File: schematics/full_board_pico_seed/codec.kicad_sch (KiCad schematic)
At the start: 26 parts, among them J10 Conn_01x01_Female, J11 Conn_01x01_Female, U6 CS4270-CZZ, X1 SG-5032CAN

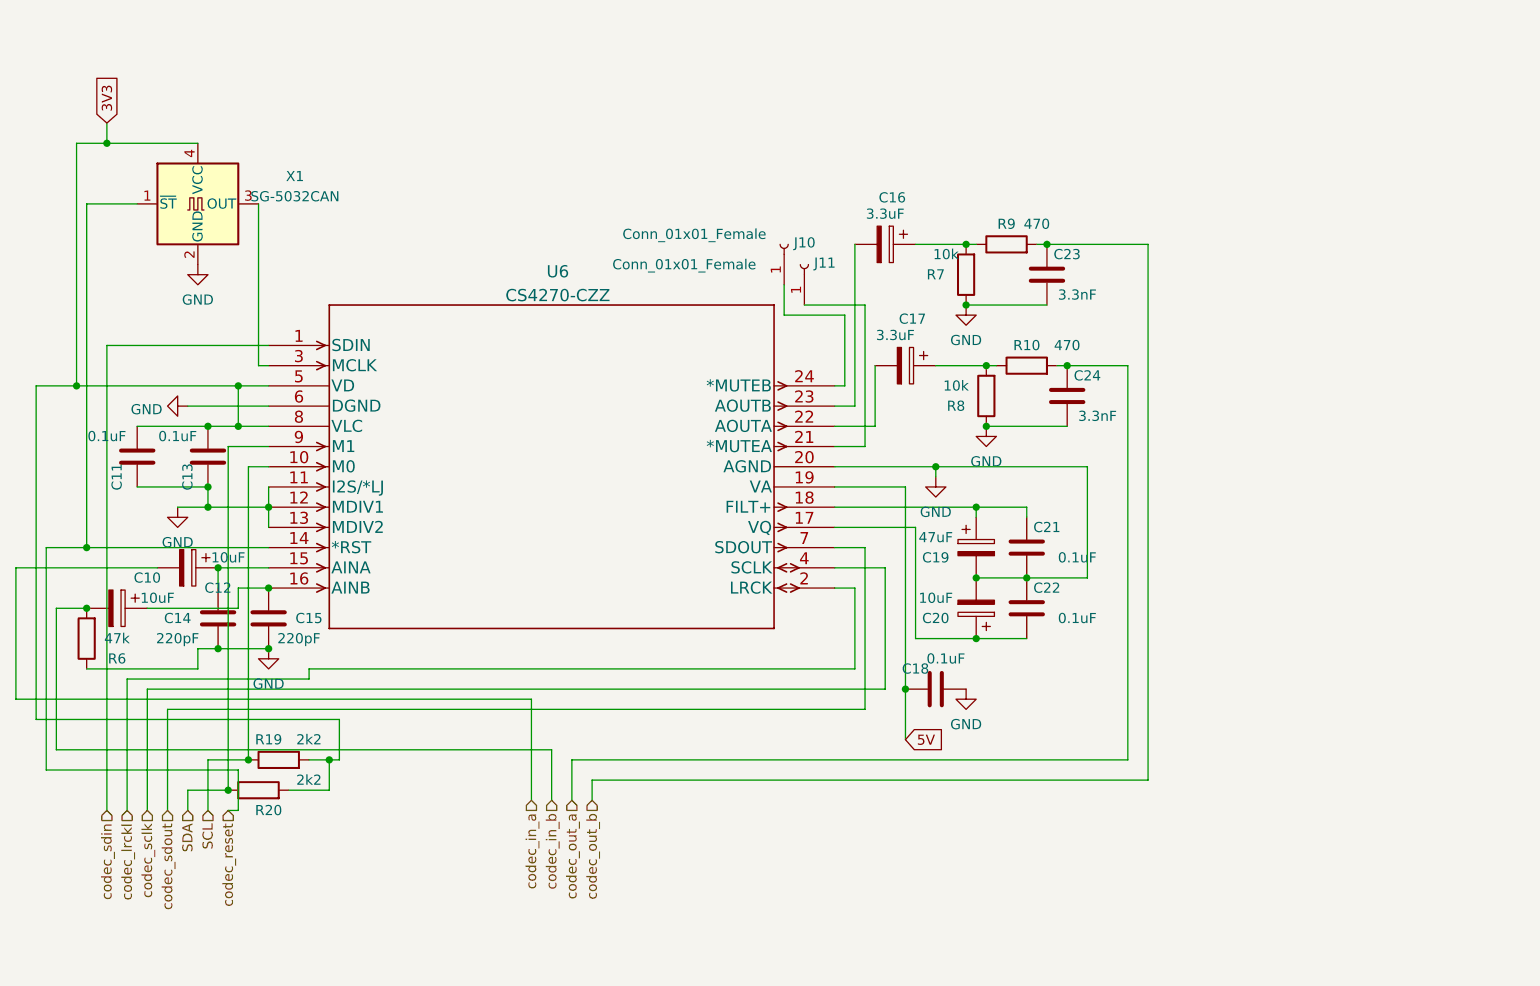
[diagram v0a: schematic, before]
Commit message: more work on full schematic: added test points
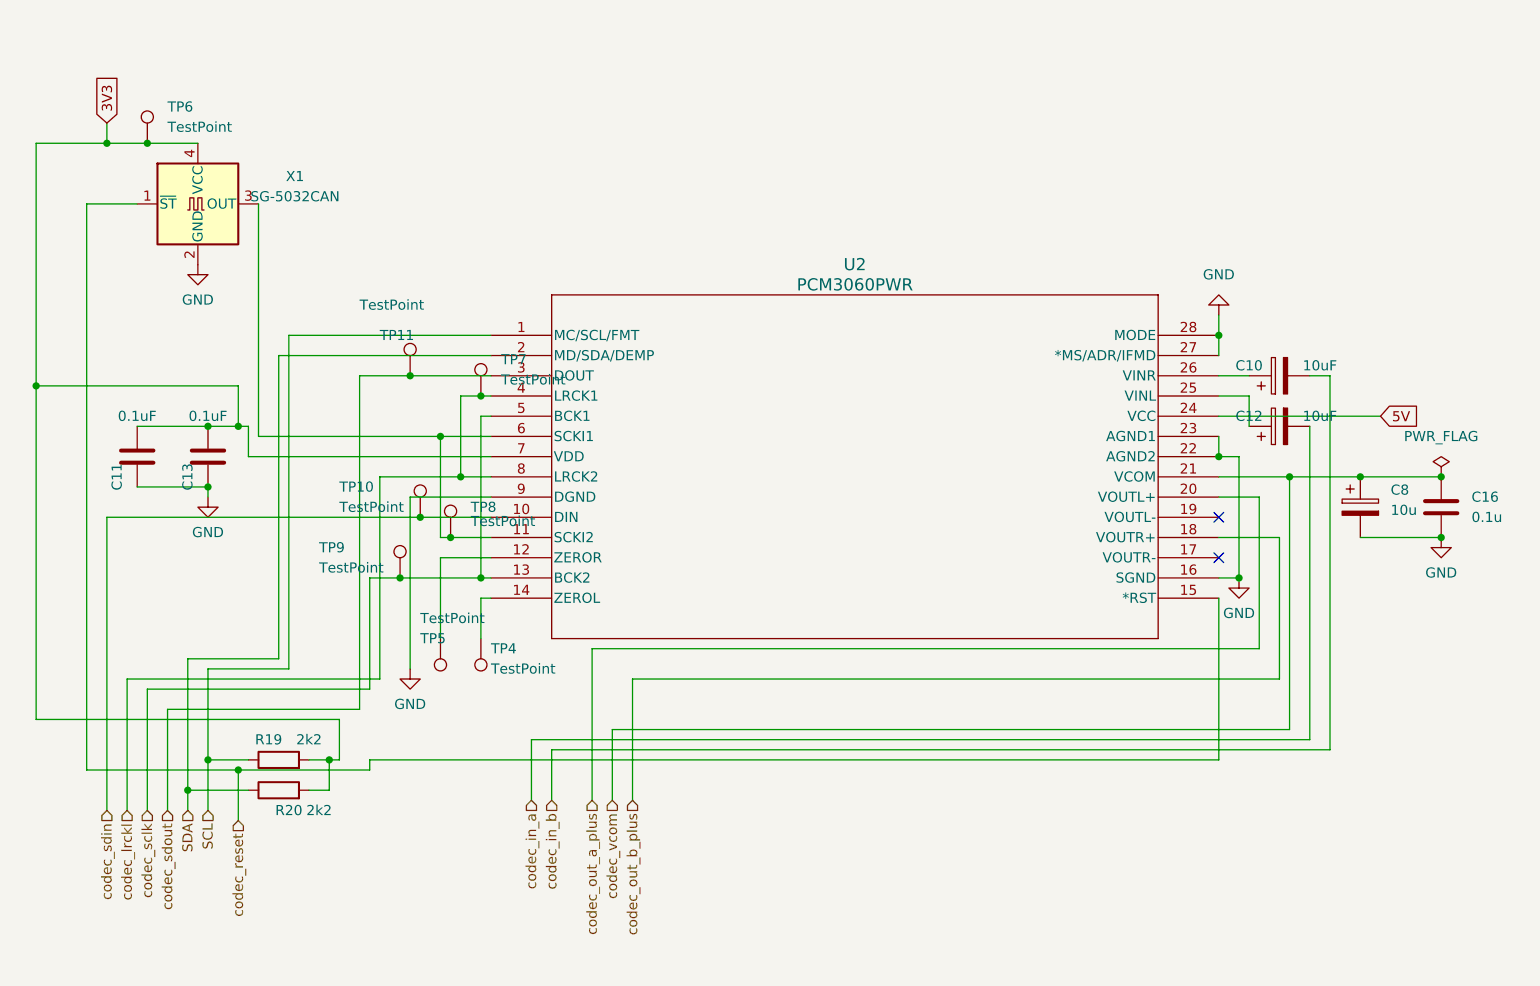
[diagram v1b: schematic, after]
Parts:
- removed C14, C15: 220pF, Capacitor_SMD:C_0603_1608Metric_Pad1.08x0.95mm_HandSolder, symbol Device:C
- removed C16, C17: 3.3uF, Capacitor_SMD:CP_Elec_4x4.5, symbol Device:C_Polarized
- removed C18, C21, C22: 0.1uF, Capacitor_SMD:C_1210_3225Metric_Pad1.33x2.70mm_HandSolder, symbol Device:C
- removed C19: 47uF, Capacitor_SMD:CP_Elec_5x5.4, symbol Device:C_Polarized
- removed C20: 10uF, Capacitor_SMD:CP_Elec_4x4.5, symbol Device:C_Polarized
- removed C23, C24: 3.3nF, Capacitor_SMD:C_0805_2012Metric_Pad1.18x1.45mm_HandSolder, symbol Device:C
- removed J10, J11: Conn_01x01_Female, Connector_Pin:Pin_D0.7mm_L6.5mm_W1.8mm_FlatFork, symbol Connector:Conn_01x01_Female
- removed R10, R9: 470, Resistor_SMD:R_0603_1608Metric_Pad0.98x0.95mm_HandSolder, symbol Device:R
- removed R6: 47k, Resistor_SMD:R_0603_1608Metric_Pad0.98x0.95mm_HandSolder, symbol Device:R
- removed R7, R8: 10k, Resistor_SMD:R_0603_1608Metric_Pad0.98x0.95mm_HandSolder, symbol Device:R
- removed U6: CS4270-CZZ, Package_SO:TSSOP-24_4.4x7.8mm_P0.65mm, symbol 2022-10-31_07-27-24:CS4270-CZZ
- added C16: 0.1u, Capacitor_SMD:C_0805_2012Metric_Pad1.18x1.45mm_HandSolder, symbol Device:C
- added C8: 10u, Capacitor_SMD:CP_Elec_4x4.5, symbol Device:C_Polarized
- added TP10, TP11, TP4, TP5, TP6, TP7, TP8, TP9: TestPoint, TestPoint:TestPoint_Pad_D1.5mm, symbol Connector:TestPoint
- added U2: PCM3060PWR, Package_SO:TSSOP-28_4.4x9.7mm_P0.65mm, symbol pcm3060:PCM3060PWR
- C11, C13: footprint Capacitor_SMD:C_1210_3225Metric_Pad1.33x2.70mm_HandSolder -> Capacitor_SMD:C_0805_2012Metric_Pad1.18x1.45mm_HandSolder
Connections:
- net 3V3: now also TP6.1, U2.7 (VDD)
- net 5V: now also U2.24 (VCC)
- net GND: now also C16.2, C8.2, U2.16 (SGND), U2.22 (AGND2), U2.23 (AGND1), U2.27 (*MS/ADR/IFMD), U2.28 (MODE), U2.9 (DGND)
- net SCL: now also U2.1 (MC/SCL/FMT)
- net SDA: now also U2.2 (MD/SDA/DEMP)
- net codec_lrckl: now also TP7.1, U2.4 (LRCK1), U2.8 (LRCK2)
- net codec_reset: now also U2.15 (*RST)
- net codec_sclk: now also TP9.1, U2.13 (BCK2), U2.5 (BCK1)
- net codec_sdin: now also TP10.1, U2.10 (DIN)
- net codec_sdout: now also TP11.1, U2.3 (DOUT)
- net at C10.1: now also U2.26 (VINR)
- net at C12.1: now also U2.25 (VINL)
- net at X1.3 (OUT): now also TP8.1, U2.11 (SCKI2), U2.6 (SCKI1)
- new net: TP5.1, U2.12 (ZEROR)
- new net: TP4.1, U2.14 (ZEROL)
- new net codec_out_a_plus: U2.20 (VOUTL+)
- new net codec_out_b_plus: U2.18 (VOUTR+)
- new net codec_vcom: C16.1, C8.1, U2.21 (VCOM)
- no-connect marks 0 -> 2
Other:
- moved on the sheet: C10, C12, R20

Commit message: worked on schematics
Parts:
- C16: value 0.1u -> 0.1uF
- C8: value 10u -> 10uF
- TP10, TP11, TP4, TP5, TP6, TP7, TP8, TP9: now left out of the parts list
- X1: value SG-5032CAN -> SG-5032CAN 12.288MHz
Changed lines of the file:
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@@
 		(shape input)
 		(at 142.24 121.92 270)
-		(fields_autoplaced yes)
 		(effects
 			(font
@@
 		(shape input)
 		(at 91.44 123.19 270)
-		(fields_autoplaced yes)
 		(effects
 			(font
@@
 		(shape input)
 		(at 102.87 124.46 270)
-		(fields_autoplaced yes)
 		(effects
 			(font
@@
 		(shape input)
 		(at 147.32 121.92 270)
-		(fields_autoplaced yes)
 		(effects
 			(font
@@
 		(shape input)
 		(at 86.36 123.19 270)
-		(fields_autoplaced yes)
 		(effects
 			(font
@@
 		(shape input)
 		(at 149.86 121.92 270)
-		(fields_autoplaced yes)
 		(effects
 			(font
@@
 		(shape input)
 		(at 99.06 123.19 270)
-		(fields_autoplaced yes)
 		(effects
 			(font
@@
 		(shape input)
 		(at 93.98 123.19 270)
-		(fields_autoplaced yes)
 		(effects
 			(font
@@
 		(shape input)
 		(at 96.52 123.19 270)
-		(fields_autoplaced yes)
 		(effects
 			(font
@@
 		(shape input)
 		(at 152.4 121.92 270)
-		(fields_autoplaced yes)
 		(effects
 			(font
@@
 		(shape input)
 		(at 88.9 123.19 270)
-		(fields_autoplaced yes)
 		(effects
 			(font
@@
 		(shape input)
 		(at 139.7 121.92 270)
-		(fields_autoplaced yes)
 		(effects
 			(font
@@
 		(unit 1)
 		(exclude_from_sim no)
-		(in_bom yes)
+		(in_bom no)
 		(on_board yes)
 		(dnp no)
@@
 		(unit 1)
 		(exclude_from_sim no)
-		(in_bom yes)
+		(in_bom no)
 		(on_board yes)
 		(dnp no)
@@
 		(unit 1)
 		(exclude_from_sim no)
-		(in_bom yes)
+		(in_bom no)
 		(on_board yes)
 		(dnp no)
@@
 		(unit 1)
 		(exclude_from_sim no)
-		(in_bom yes)
+		(in_bom no)
 		(on_board yes)
 		(dnp no)
@@
 		(fields_autoplaced yes)
 		(property "Reference" "C16"
-			(at 257.81 83.82 0)
+			(at 257.81 83.8199 0)
 			(effects
 				(font
@@
 			)
 		)
-		(property "Value" "0.1u"
-			(at 257.81 86.36 0)
+		(property "Value" "0.1uF"
+			(at 257.81 86.3599 0)
 			(effects
 				(font
@@
 		(unit 1)
 		(exclude_from_sim no)
-		(in_bom yes)
+		(in_bom no)
 		(on_board yes)
 		(dnp no)
@@
 		(unit 1)
 		(exclude_from_sim no)
-		(in_bom yes)
+		(in_bom no)
 		(on_board yes)
 		(dnp no)
@@
 		(unit 1)
 		(exclude_from_sim no)
-		(in_bom yes)
+		(in_bom no)
 		(on_board yes)
 		(dnp no)
@@
 		(fields_autoplaced yes)
 		(property "Reference" "C8"
-			(at 247.65 82.931 0)
+			(at 247.65 82.9309 0)
 			(effects
 				(font
@@
 			)
 		)
-		(property "Value" "10u"
-			(at 247.65 85.471 0)
+		(property "Value" "10uF"
+			(at 247.65 85.4709 0)
 			(effects
 				(font
@@
 		(fields_autoplaced yes)
 		(property "Reference" "X1"
-			(at 110.0009 43.5316 0)
-			(effects
-				(font
-					(size 1.27 1.27)
-				)
-			)
-		)
-		(property "Value" "SG-5032CAN"
-			(at 110.0009 46.0685 0)
+			(at 116.84 40.6714 0)
+			(effects
+				(font
+					(size 1.27 1.27)
+				)
+			)
+		)
+		(property "Value" "SG-5032CAN 12.288MHz"
+			(at 116.84 43.2114 0)
 			(effects
 				(font
@@
 		(unit 1)
 		(exclude_from_sim no)
-		(in_bom yes)
-		(on_board yes)
-		(dnp no)
+		(in_bom no)
+		(on_board yes)
+		(dnp no)
